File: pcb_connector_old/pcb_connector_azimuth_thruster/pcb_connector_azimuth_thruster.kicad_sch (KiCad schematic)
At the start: 14 parts

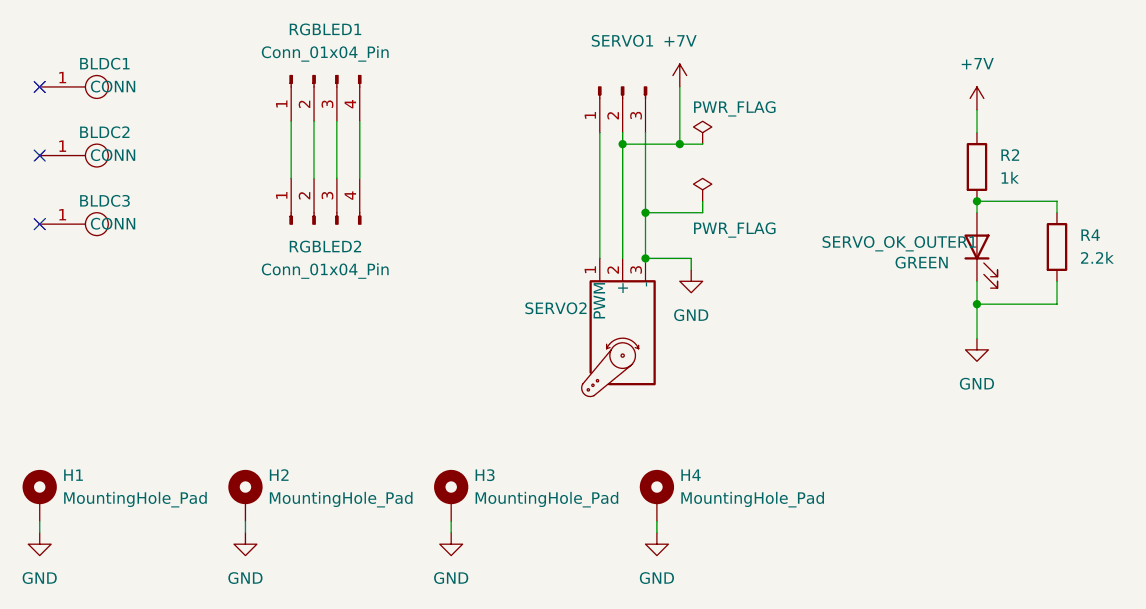
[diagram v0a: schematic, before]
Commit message: 旧基板防水をpcb_connector_oldに移動
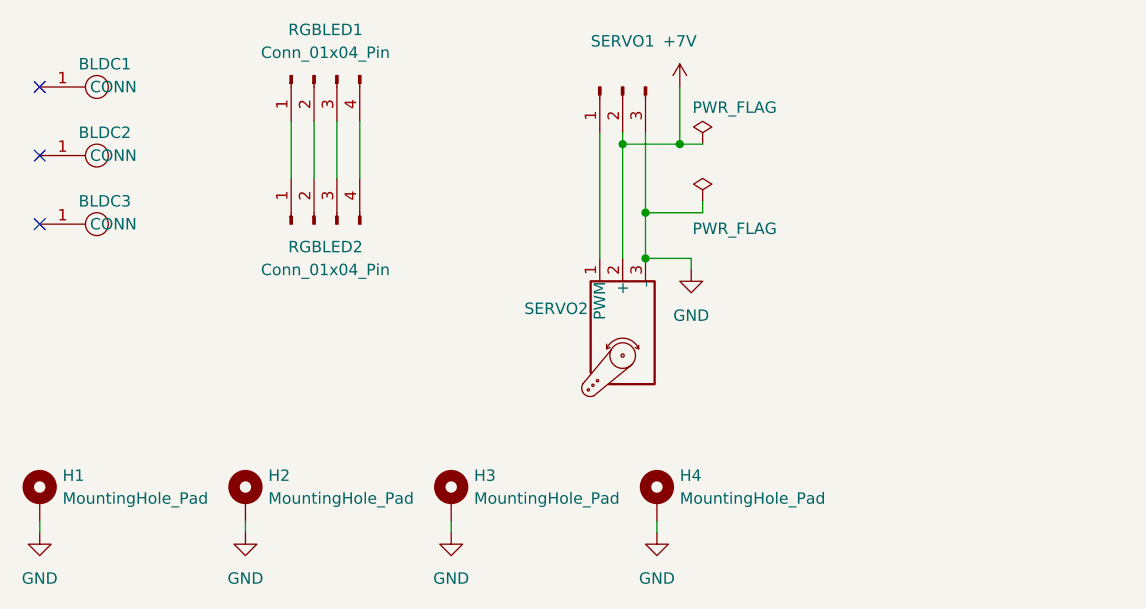
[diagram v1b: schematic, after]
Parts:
- removed R2: 1k, Resistor_SMD:R_0603_1608Metric_Pad0.98x0.95mm_HandSolder, symbol Device:R
- removed R4: 2.2k, Resistor_SMD:R_0603_1608Metric_Pad0.98x0.95mm_HandSolder, symbol Device:R
- removed SERVO_OK_OUTER1: GREEN, LED_SMD:LED_0805_2012Metric_Pad1.15x1.40mm_HandSolder, symbol Device:LED
- RGBLED1: footprint Connector_JST:JST_XA_B04B-XASK-1_1x04_P2.50mm_Vertical -> Connector_PinHeader_2.54mm:PinHeader_1x04_P2.54mm_Vertical
- SERVO1: footprint Connector_JST:JST_XA_B03B-XASK-1_1x03_P2.50mm_Vertical -> Connector_PinSocket_2.54mm:PinSocket_1x03_P2.54mm_Vertical
